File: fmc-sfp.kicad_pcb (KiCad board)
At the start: 2 copper layers, 89.5 x 70 mm, 43 parts, among them J1 ASP-134604-01, J2 SFP+, J3 SFP+, J4 132134, J5 132134, J6 132134, J7 132134, SW1 SW_DIP_x04, U1 MAX9113EKA_TT, U2 MAX9113EKA_TT

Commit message: exclude test points from BOM
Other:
- board text added: "Git Commit:Rev0a-16-g620039f-dirty"
- board text removed: "Git Commit:"
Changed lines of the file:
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@@
 		(sheetname "Root")
 		(sheetfile "fmc-sfp.kicad_sch")
-		(attr exclude_from_pos_files)
+		(attr exclude_from_pos_files exclude_from_bom)
 		(fp_circle
 			(center 0 0)
@@
 		(sheetname "Root")
 		(sheetfile "fmc-sfp.kicad_sch")
-		(attr exclude_from_pos_files)
+		(attr exclude_from_pos_files exclude_from_bom)
 		(fp_circle
 			(center 0 0)
@@
 		(sheetname "Root")
 		(sheetfile "fmc-sfp.kicad_sch")
-		(attr exclude_from_pos_files)
+		(attr exclude_from_pos_files exclude_from_bom)
 		(fp_circle
 			(center 0 0)
@@
 		(sheetname "Root")
 		(sheetfile "fmc-sfp.kicad_sch")
-		(attr exclude_from_pos_files)
+		(attr exclude_from_pos_files exclude_from_bom)
 		(fp_circle
 			(center 0 0)
@@
 		(sheetname "Root")
 		(sheetfile "fmc-sfp.kicad_sch")
-		(attr exclude_from_pos_files)
+		(attr exclude_from_pos_files exclude_from_bom)
 		(fp_circle
 			(center 0 0)
@@
 		(sheetname "Root")
 		(sheetfile "fmc-sfp.kicad_sch")
-		(attr exclude_from_pos_files)
+		(attr exclude_from_pos_files exclude_from_bom)
 		(fp_circle
 			(center 0 0)
@@
 		(sheetname "Root")
 		(sheetfile "fmc-sfp.kicad_sch")
-		(attr exclude_from_pos_files)
+		(attr exclude_from_pos_files exclude_from_bom)
 		(fp_circle
 			(center 0 0)
@@
 		(sheetname "Root")
 		(sheetfile "fmc-sfp.kicad_sch")
-		(attr exclude_from_pos_files)
+		(attr exclude_from_pos_files exclude_from_bom)
 		(fp_circle
 			(center 0 0)
@@
 		)
 	)
-	(gr_text "Git Commit:"
+	(gr_text "Git Commit:Rev0a-16-g620039f-dirty"
 		(at 100.9 89.9 0)
 		(layer "F.SilkS")

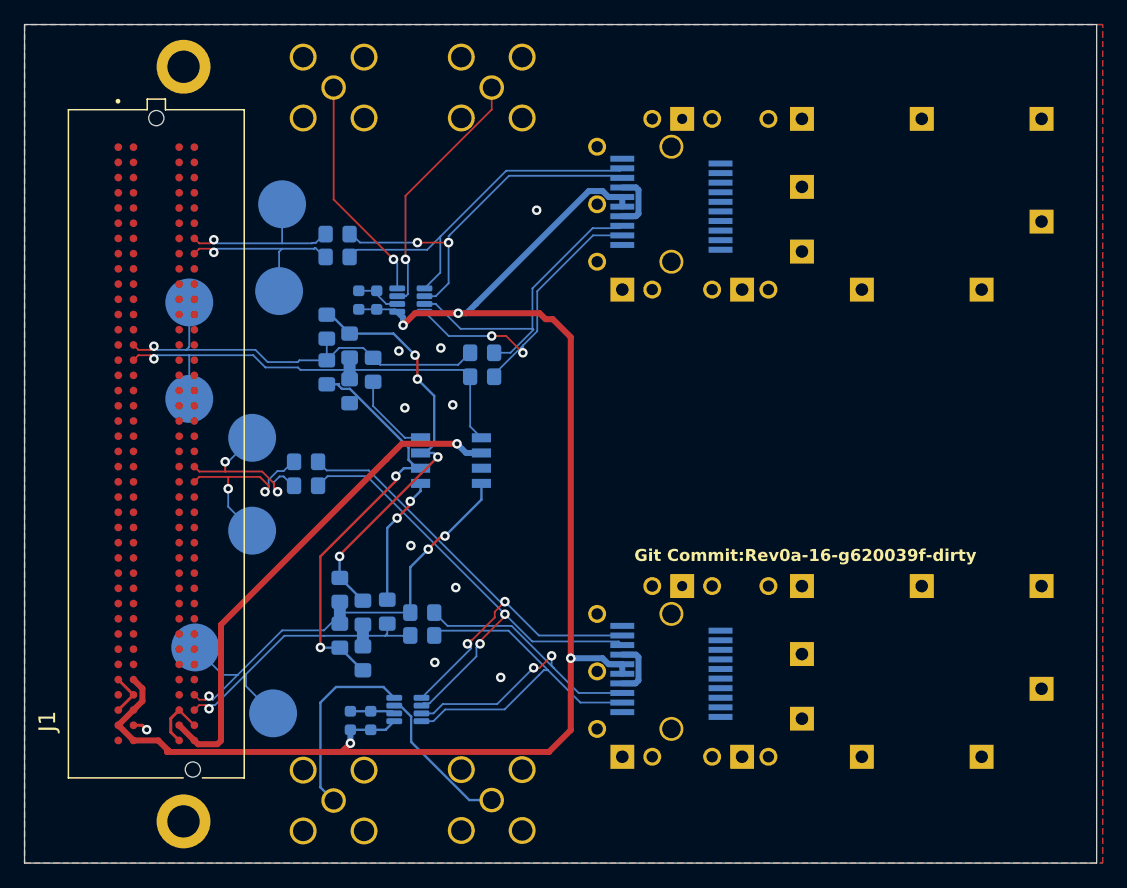
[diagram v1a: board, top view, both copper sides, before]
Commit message: asthetic cleanup, add ground testpoint
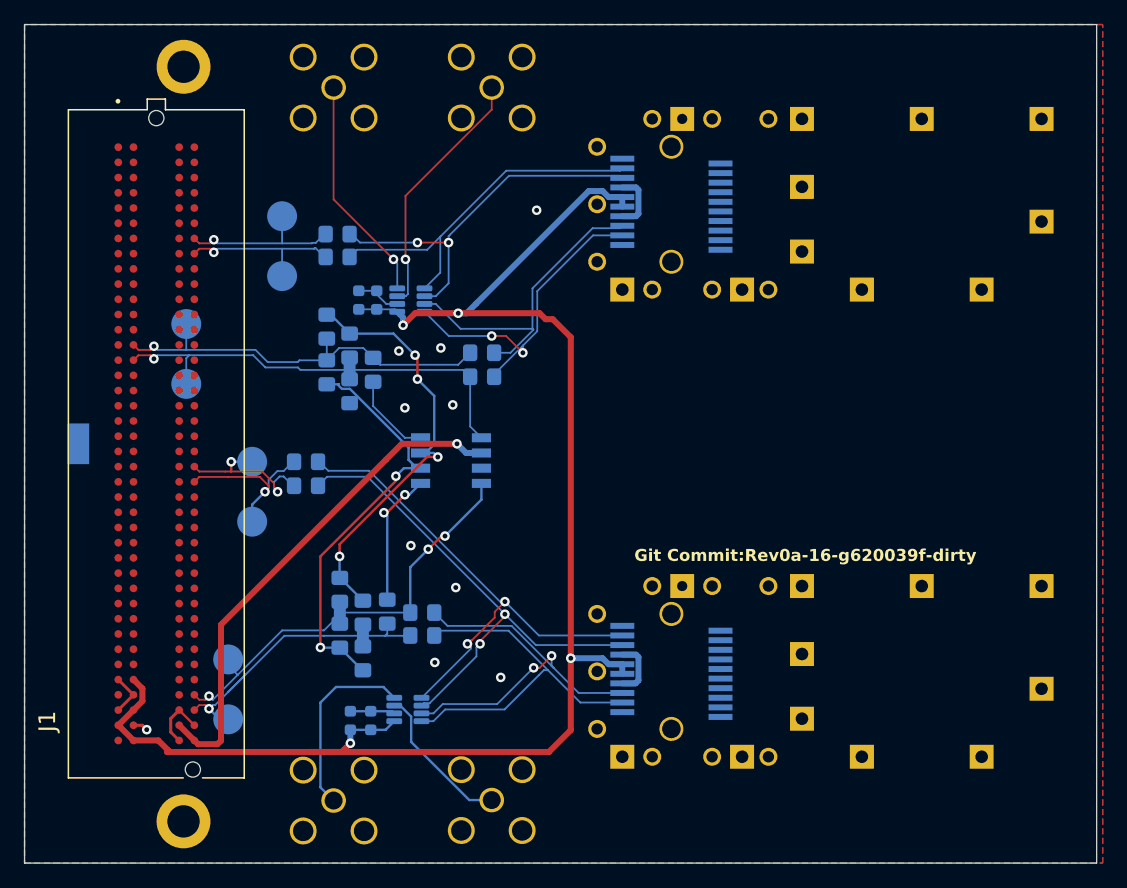
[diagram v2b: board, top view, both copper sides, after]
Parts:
- added TP9: GND, TestPoint:TestPoint_Keystone_5015_Micro-Minature, B.Cu at (54.5, 80.0)
- TP1, TP2, TP3, TP4, TP5, TP6, TP7, TP8: footprint TestPoint:TestPoint_Pad_D4.0mm -> TestPoint:TestPoint_Pad_D2.5mm
- moved TP8 3.78 mm to (67.0, 103.0)
- moved TP7 2.93 mm to (67.0, 98.0)
- moved TP5 2.00 mm to (69.0, 81.5)
- moved TP1 1.82 mm to (63.5, 70.0)
- moved TP2 1.27 mm to (63.5, 75.0)
- moved TP4 1.27 mm to (71.5, 66.0)
- moved TP3 1.00 mm to (71.5, 61.0)
- moved TP6 0.75 mm to (69.0, 86.5)
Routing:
- net /FMC_LA32_P: track 41.2 -> 38.3 mm
- net /FMC_LA19_N: track 16.5 -> 14.1 mm, vias 2 -> 1
- net /FMC_LA09_P: track 36.3 -> 34.4 mm
- net /FMC_LA19_P: track 15.1 -> 13.7 mm
- net /FMC_LA02_N: track 15.3 -> 14.2 mm
- net /FMC_LA09_N: track 40.2 -> 39.1 mm
- net /FMC_LA02_P: track 15.0 -> 14.0 mm
- net Net-(R6-Pad1): track 10.9 -> 11.5 mm
- net /bias_hi: track 36.1 -> 36.6 mm

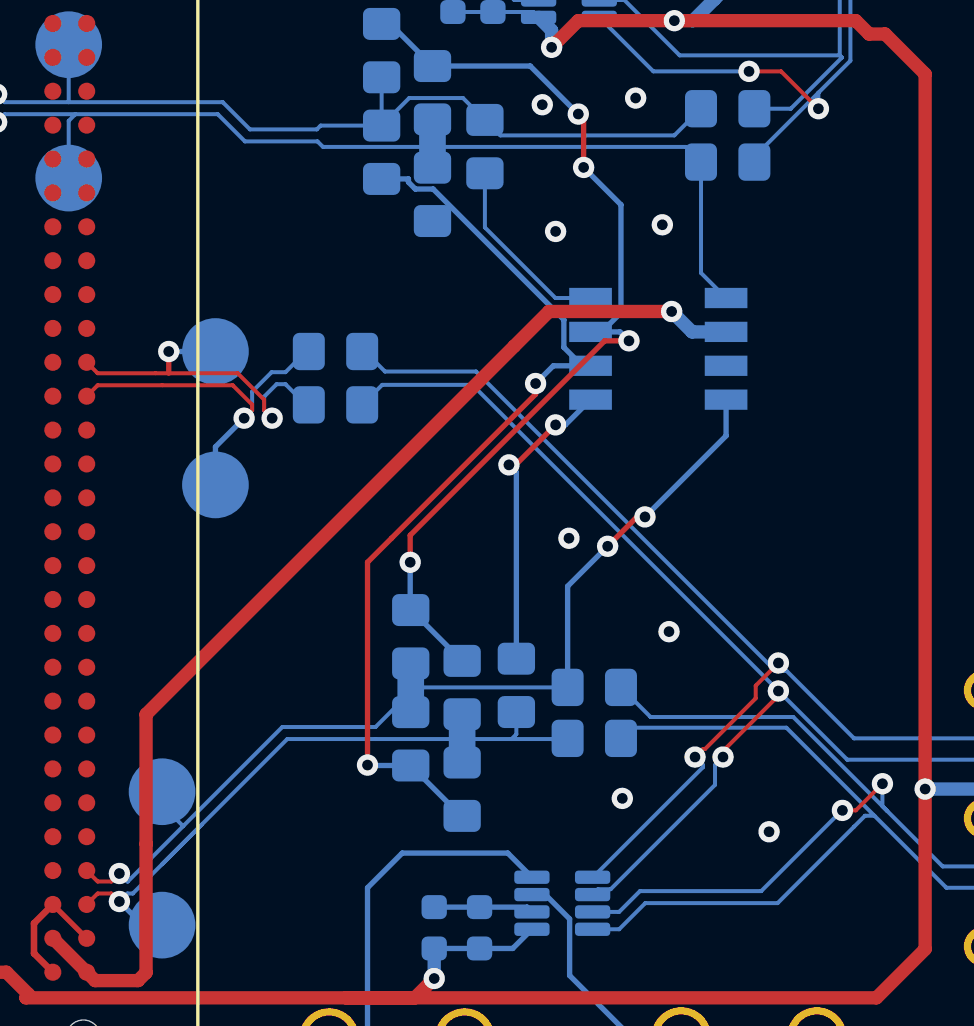
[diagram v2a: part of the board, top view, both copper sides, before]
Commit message: set SW1 part number
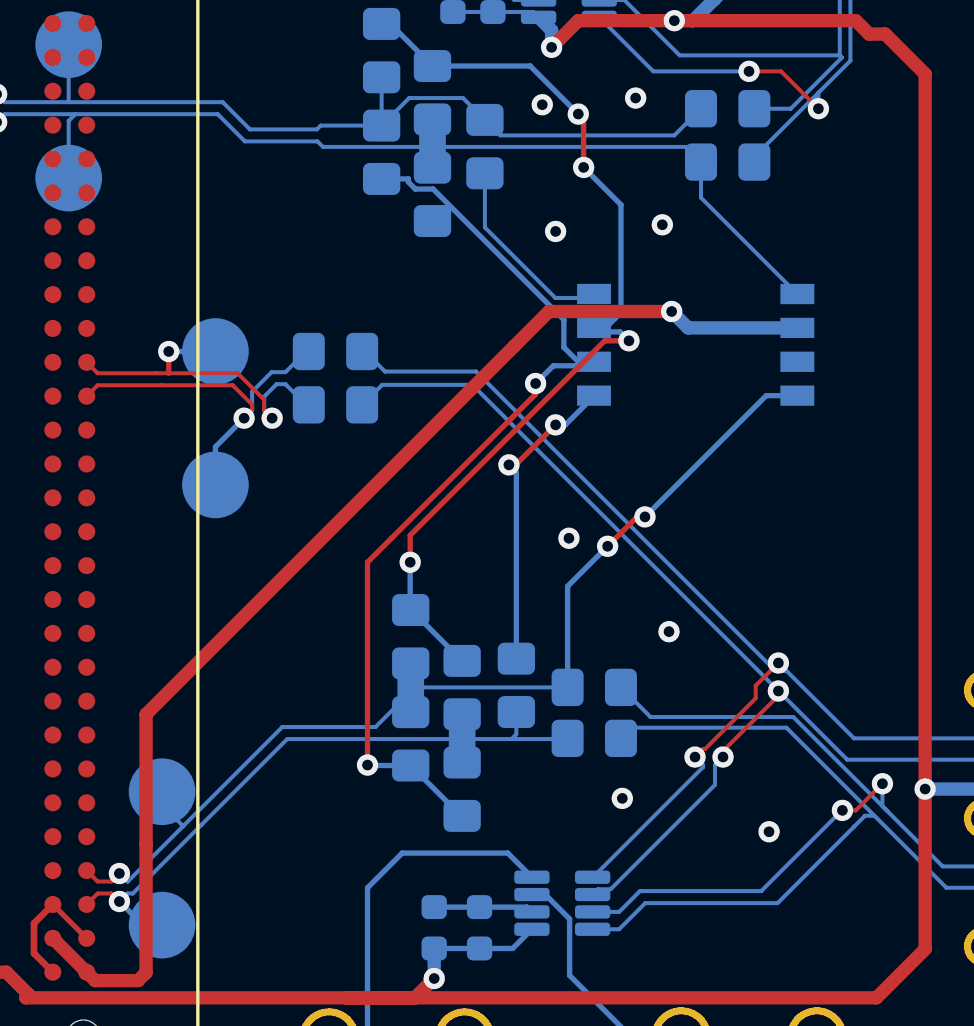
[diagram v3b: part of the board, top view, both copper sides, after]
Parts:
- SW1: footprint Button_Switch_SMD:SW_DIP_SPSTx04_Slide_Copal_CHS-04A_W5.08mm_P1.27mm_JPin -> Button_Switch_SMD:SW_DIP_SPSTx04_Slide_KingTek_DSHP04TS_W7.62mm_P1.27mm
- moved G*** 5.10 mm to (123.2, 78.8)
- moved SW1 1.41 mm to (87.0, 81.2)
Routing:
- net VADJ: track 42.3 -> 44.9 mm
- net /FMC_LA32_N: track 28.0 -> 25.9 mm
- net /FMC_LA32_P: track 38.3 -> 40.3 mm
- net /FMC_LA09_N: track 39.1 -> 40.0 mm
